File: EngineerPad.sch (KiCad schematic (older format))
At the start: 70 parts, among them J1 AVR ISP 6, J2 USB_A, SW1 SW_Push, SW10 SW_Push, SW11 SW_Push, SW12 SW_Push, SW13 SW_Push, SW14 SW_Push, SW15 SW_Push, SW16 SW_Push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

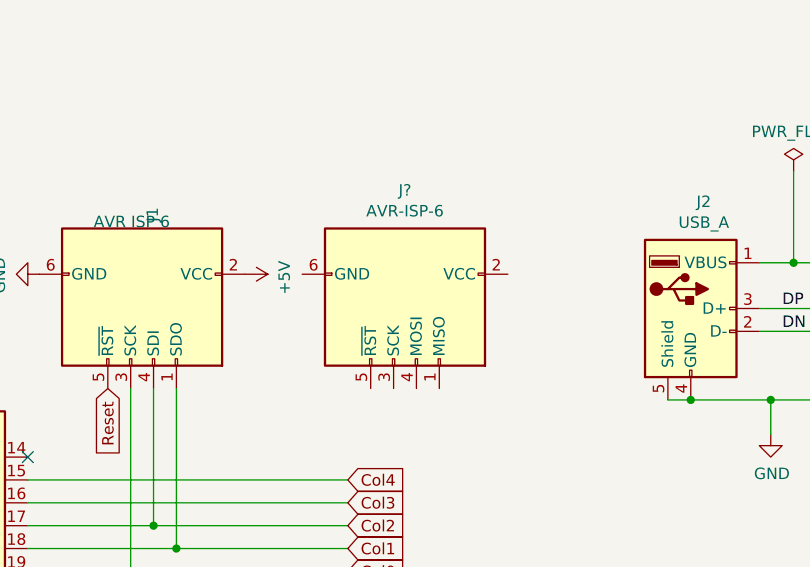
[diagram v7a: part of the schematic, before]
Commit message: fix minor wiring
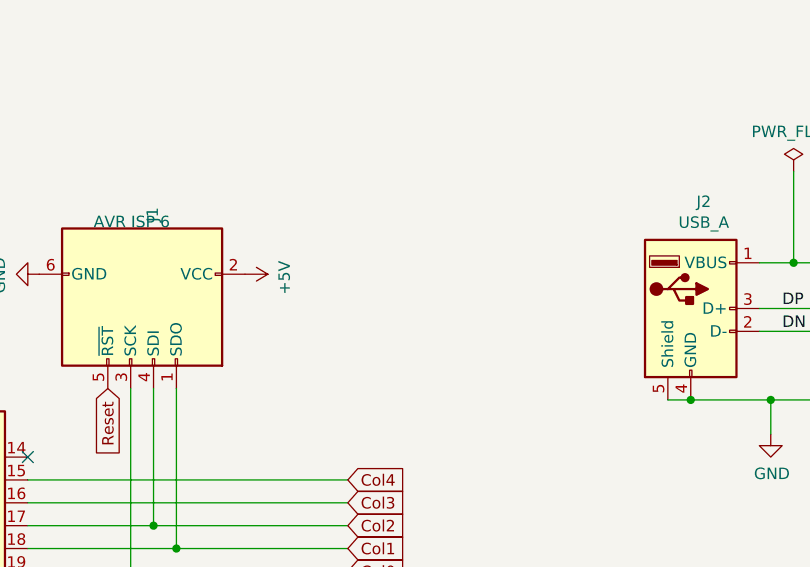
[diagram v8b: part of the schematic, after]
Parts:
- removed J?: AVR-ISP-6, symbol Connector:AVR-ISP-6
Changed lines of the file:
@@
 Wire Wire Line
 	2450 2600 3850 2600
-$Comp
-L Connector:AVR-ISP-6 J?
-U 1 1 5F4E2942
-P 4050 1800
-F 0 "J?" V 3583 1850 50  0000 C CNN
-F 1 "AVR-ISP-6" V 3674 1850 50  0000 C CNN
-F 2 "" V 3800 1850 50  0001 C CNN
-F 3 " ~" H 2775 1250 50  0001 C CNN
-	1    4050 1800
-	0    1    1    0
-$EndComp
 $EndSCHEMATC
